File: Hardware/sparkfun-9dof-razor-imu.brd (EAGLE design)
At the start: 31.8 x 31.8 mm, 54 parts, among them J1 LiPo, J3 USD_CONNECTOR, U1 3.3V, U2 MCP73831, U3 MPU-9250", U4 ATSAMD21G-A, Y1 32.768kHz

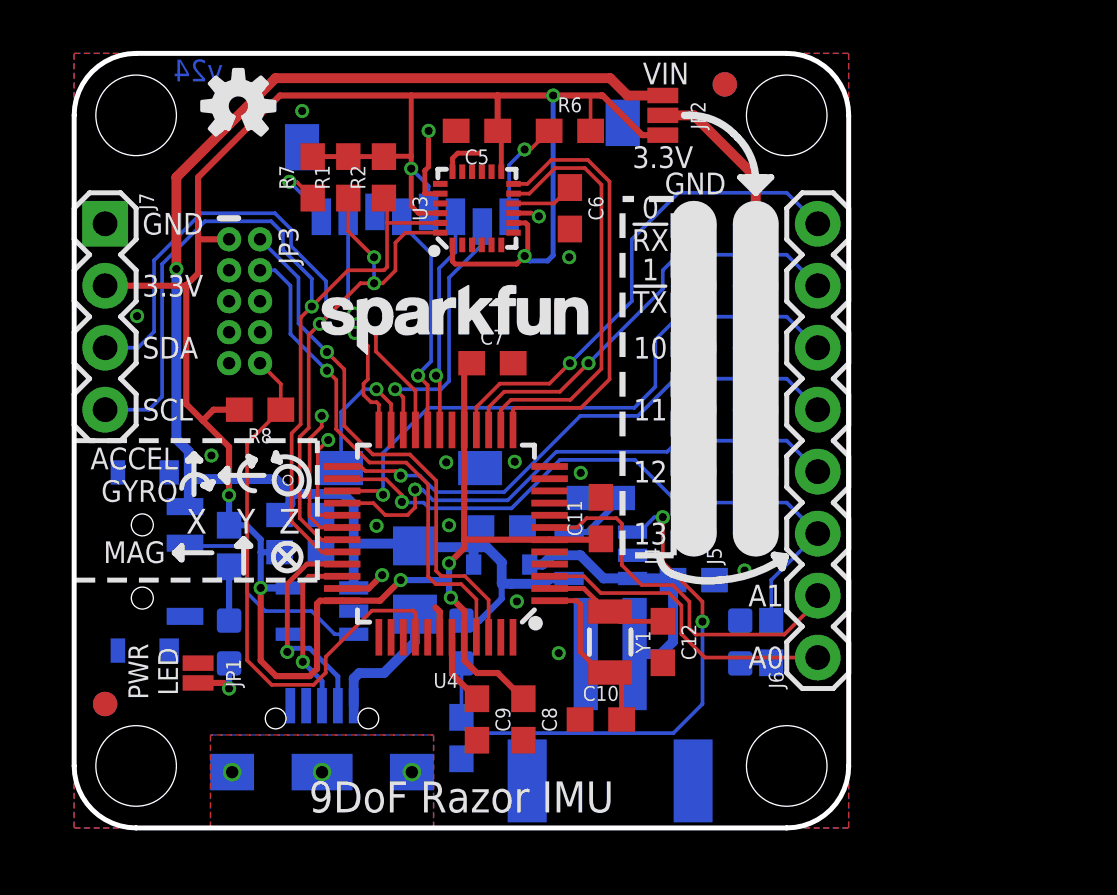
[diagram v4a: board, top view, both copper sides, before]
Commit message: Reorganizing expansion header(s), layout cleanup, PROD_ID's.
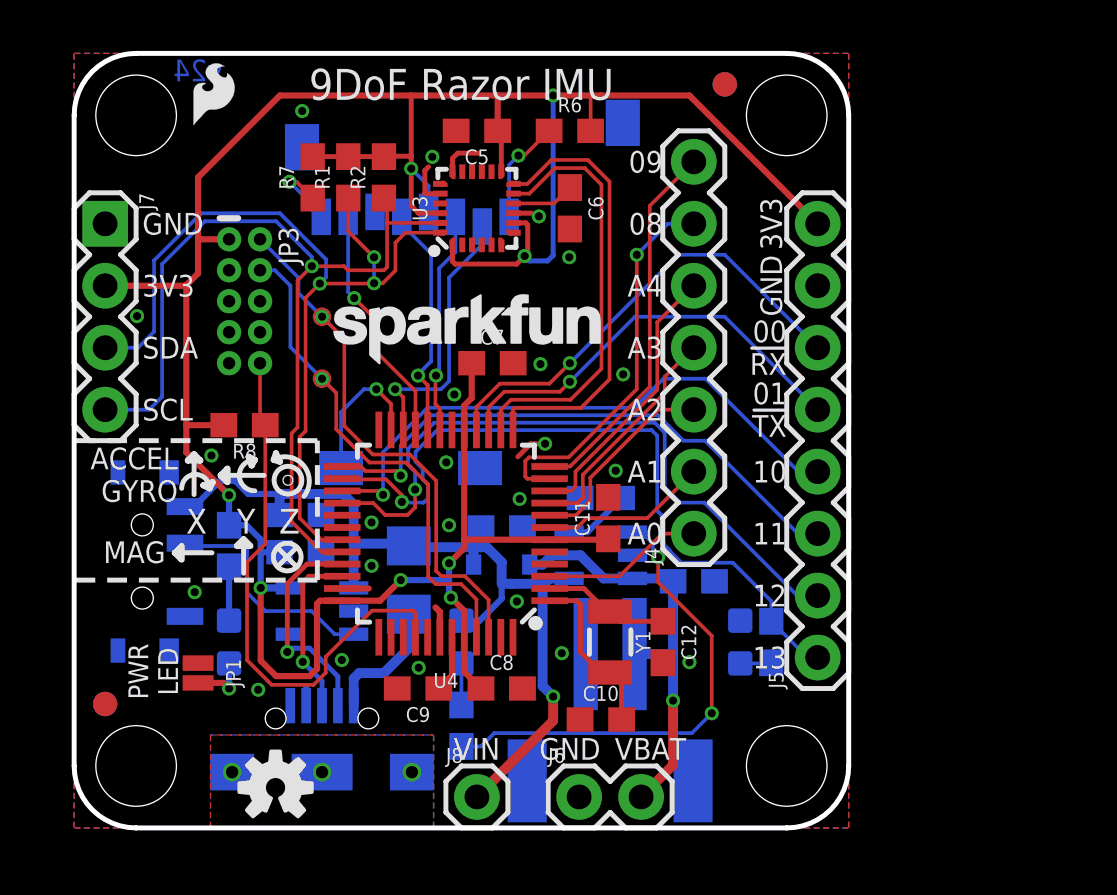
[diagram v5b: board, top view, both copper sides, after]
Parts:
- removed JP2: PWR, SparkFun-Jumpers:SMT-JUMPER_3_1-NC_PASTE_NO-SILK
- added J8: (no value), SparkFun-Connectors:1X01
- added LOGO4: SFE_LOGO_FLAME.1_INCH, SparkFun-Aesthetics:SFE_LOGO_FLAME_.1
- added TP1, TP2: TEST-POINT3, SparkFun-Connectors:PAD.03X.03
- J4: device SparkFun-Connectors:1X06_NO_SILK -> SparkFun-Connectors:1X07
- J5: device SparkFun-Connectors:1X06_NO_SILK -> SparkFun-Connectors:1X08
- J6: device SparkFun-Connectors:1X08 -> SparkFun-Connectors:1X02
- U3: value MPU-9250" -> MPU-9250
- moved LOGO2 28.0 mm to (8.26, 1.65)
- moved J6 11.3 mm to (20.7, 1.27), turned to 0 degrees
- moved J5 5.68 mm to (30.5, 6.99)
- moved C9 2.73 mm to (14.1, 5.71), turned to 180 degrees
- moved C8 1.55 mm to (17.5, 5.71), turned to 0 degrees
- moved R8 0.90 mm to (6.99, 16.5)
- moved LOGO3 0.63 mm to (10.2, 18.5)
- moved R5 0.51 mm to (15.9, 4.19)
- moved C11 0.30 mm to (21.9, 12.7)
- moved F1 0.25 mm to (13.7, 10.2)
- moved C4 0.05 mm to (25.4, 10.1)
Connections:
- removed net N$10: C4.1, D1.A, J1.2, U2.3
- removed net N$6: J5.1, J5.2, J5.3, J5.4, J5.5, J5.6, JP2.2
- new net A2: J4.3, U4.8
- new net A3: J4.4, U4.9
- new net A4: J4.5, U4.10
- new net A5: U4.47
- new net D8: J4.6, U4.11
- new net D9: J4.7, U4.12
- new net ID: J2.ID
- new net V_BATT: C4.1, D1.A, J1.2, J6.2, U2.3
- net 3.3V: now also J5.8; no longer JP2.3
- net A0: now also J4.1; no longer J6.1
- net A1: now also J4.2; no longer J6.2
- net D0/RXI: now also J5.6; no longer J6.8
- net D1/TXO: now also J5.5; no longer J6.7
- net D10: now also J5.4; no longer J6.6
- net D11: now also J5.3; no longer J6.5
- net D12: now also J5.2; no longer J6.4
- net D13: now also J5.1; no longer J6.3
- net GND: now also J5.7, J6.1; no longer J4.1, J4.2, J4.3, J4.4, J4.5, J4.6
- net SWCLK: now also TP1.P$1
- net SWDIO: now also TP2.P$1
- net VIN: now also J8.1; no longer JP2.1
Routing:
- net VIN: track 62.3 -> 36.6 mm
- net N$6: track 19.5 -> 0.00 mm
- net V_BATT: track 0.00 -> 17.4 mm, vias 0 -> 1
- net D8: track 0.00 -> 15.8 mm, vias 0 -> 1
- net D9: track 0.00 -> 15.4 mm
- net A4: track 0.00 -> 11.4 mm
- net N$10: track 10.8 -> 0.00 mm
- net A3: track 0.00 -> 9.49 mm
- net A1: track 15.6 -> 6.86 mm
- net A2: track 0.00 -> 8.25 mm
- net A0: track 13.1 -> 6.63 mm
- net 3.3V: track 114.6 -> 121.0 mm
- net D7: track 5.86 -> 0.00 mm, vias 1 -> 0
- net D12: track 22.3 -> 27.3 mm
- net D5: track 4.67 -> 0.00 mm, vias 1 -> 0
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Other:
- board text added: "00 !RX"
- board text added: "01 !TX"
- board text added: "08"
- board text added: "09"
- board text added: "3V3"
- board text added: "A2"
- board text added: "A3"
- board text added: "A4"
- board text added: "VBAT"
- board text removed: "0 !RX"
- board text removed: "1 !TX"
- board text removed: "VBUS"
